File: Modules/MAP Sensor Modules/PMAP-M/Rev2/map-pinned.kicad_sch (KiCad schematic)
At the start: 6 parts, among them IC1 MPXH6400a, J1 Conn_02x03_Odd_Even

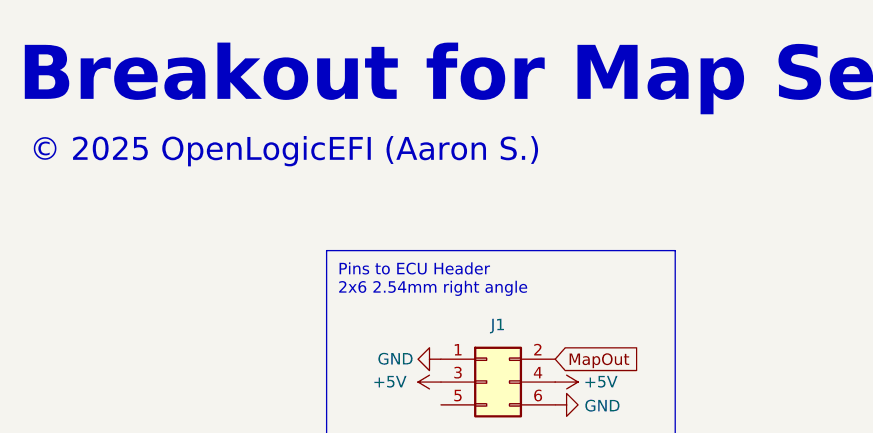
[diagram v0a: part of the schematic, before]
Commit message: INJ N-fet upload - Date corrections
N-Fet Initial Upload, recent upload date corrections.
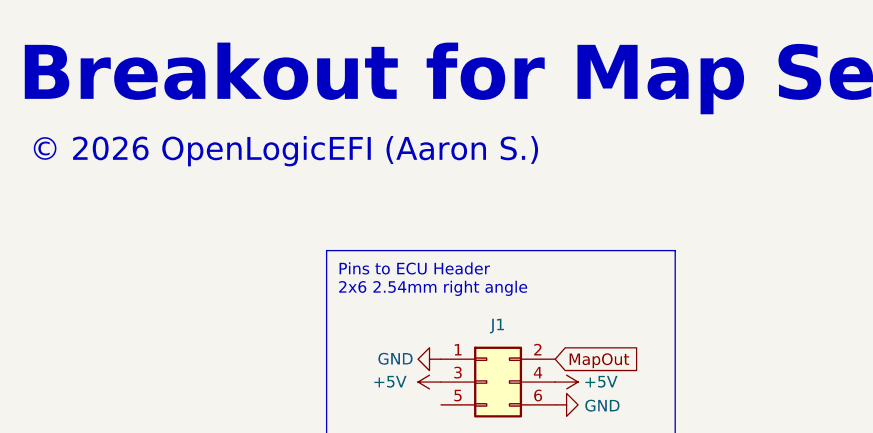
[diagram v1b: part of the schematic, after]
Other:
- note added: "© 2026 OpenLogicEFI (Aaron S.)"
- note removed: "© 2025 OpenLogicEFI (Aaron S.)"
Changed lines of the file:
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@@
 	(title_block
 		(title "PMAP-M")
-		(date "2025-05-18")
+		(date "2026-05-06")
 		(rev "M (Map Only)")
 		(company "OpenLogicEFI")
@@
 		)
 	)
-	(text "© 2025 OpenLogicEFI (Aaron S.)"
+	(text "© 2026 OpenLogicEFI (Aaron S.)"
 		(exclude_from_sim no)
 		(at 99.06 60.96 0)
